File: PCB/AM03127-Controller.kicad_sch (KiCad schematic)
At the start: 13 parts, among them U1 XIAO-ESP32-C3-DIP, U2 MAX3232, U3 AMS1117 5.0

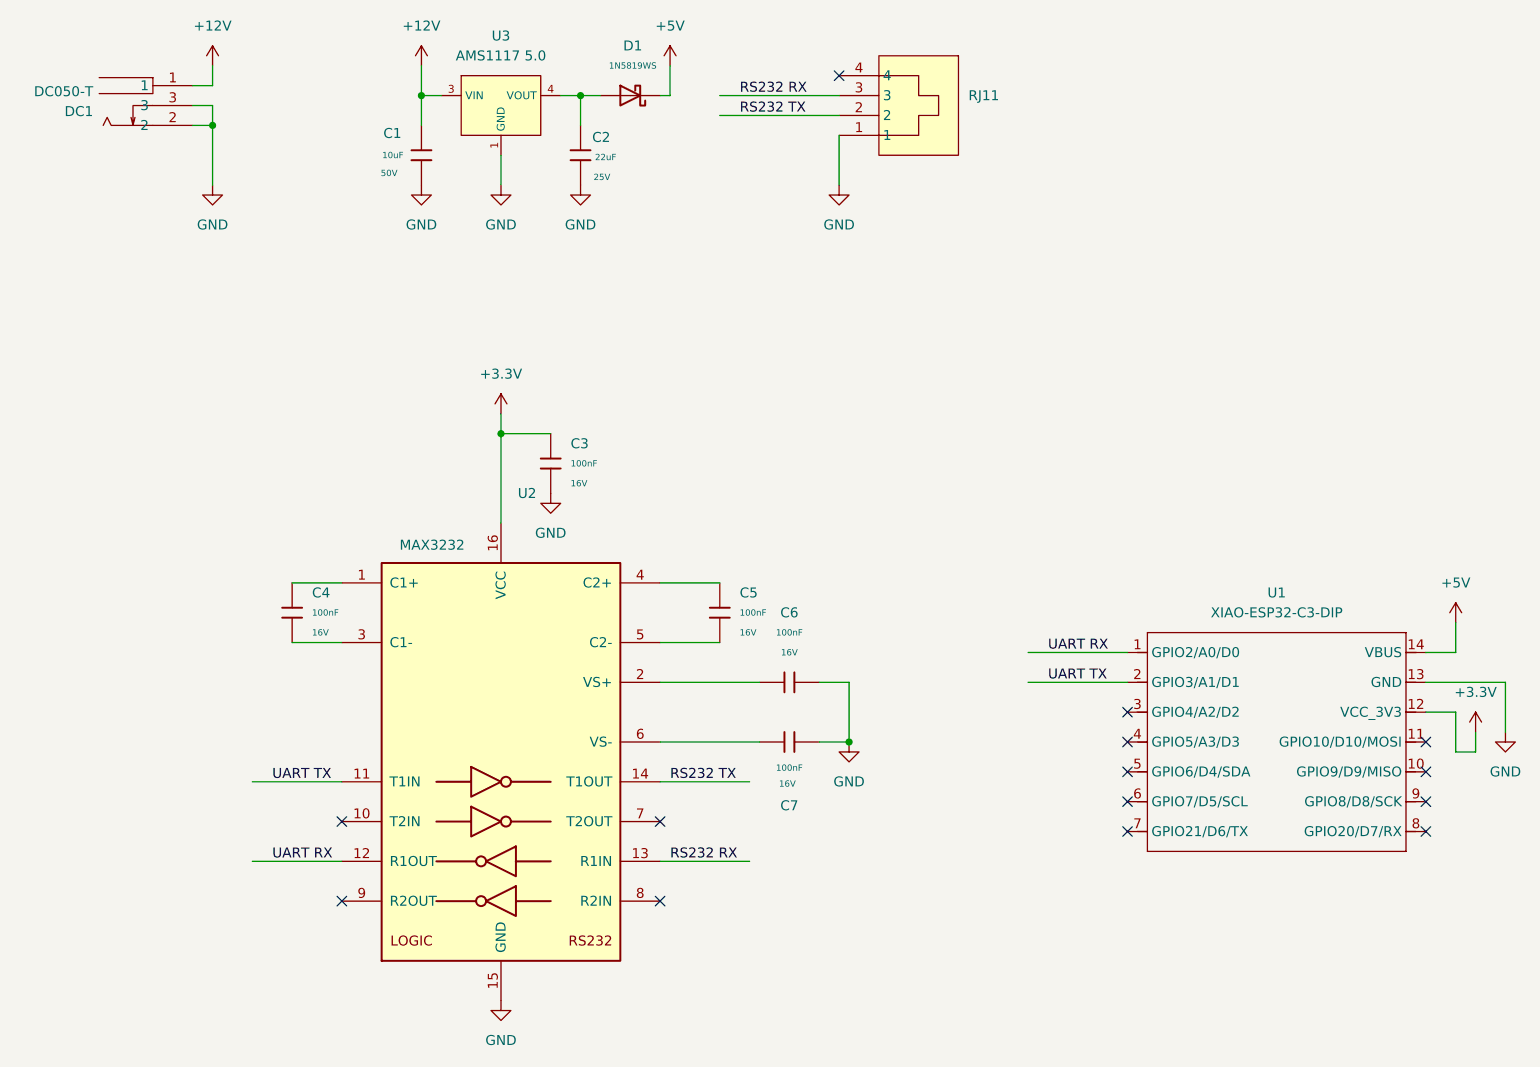
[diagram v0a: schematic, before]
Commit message: Refactor LDO to Buckconverter
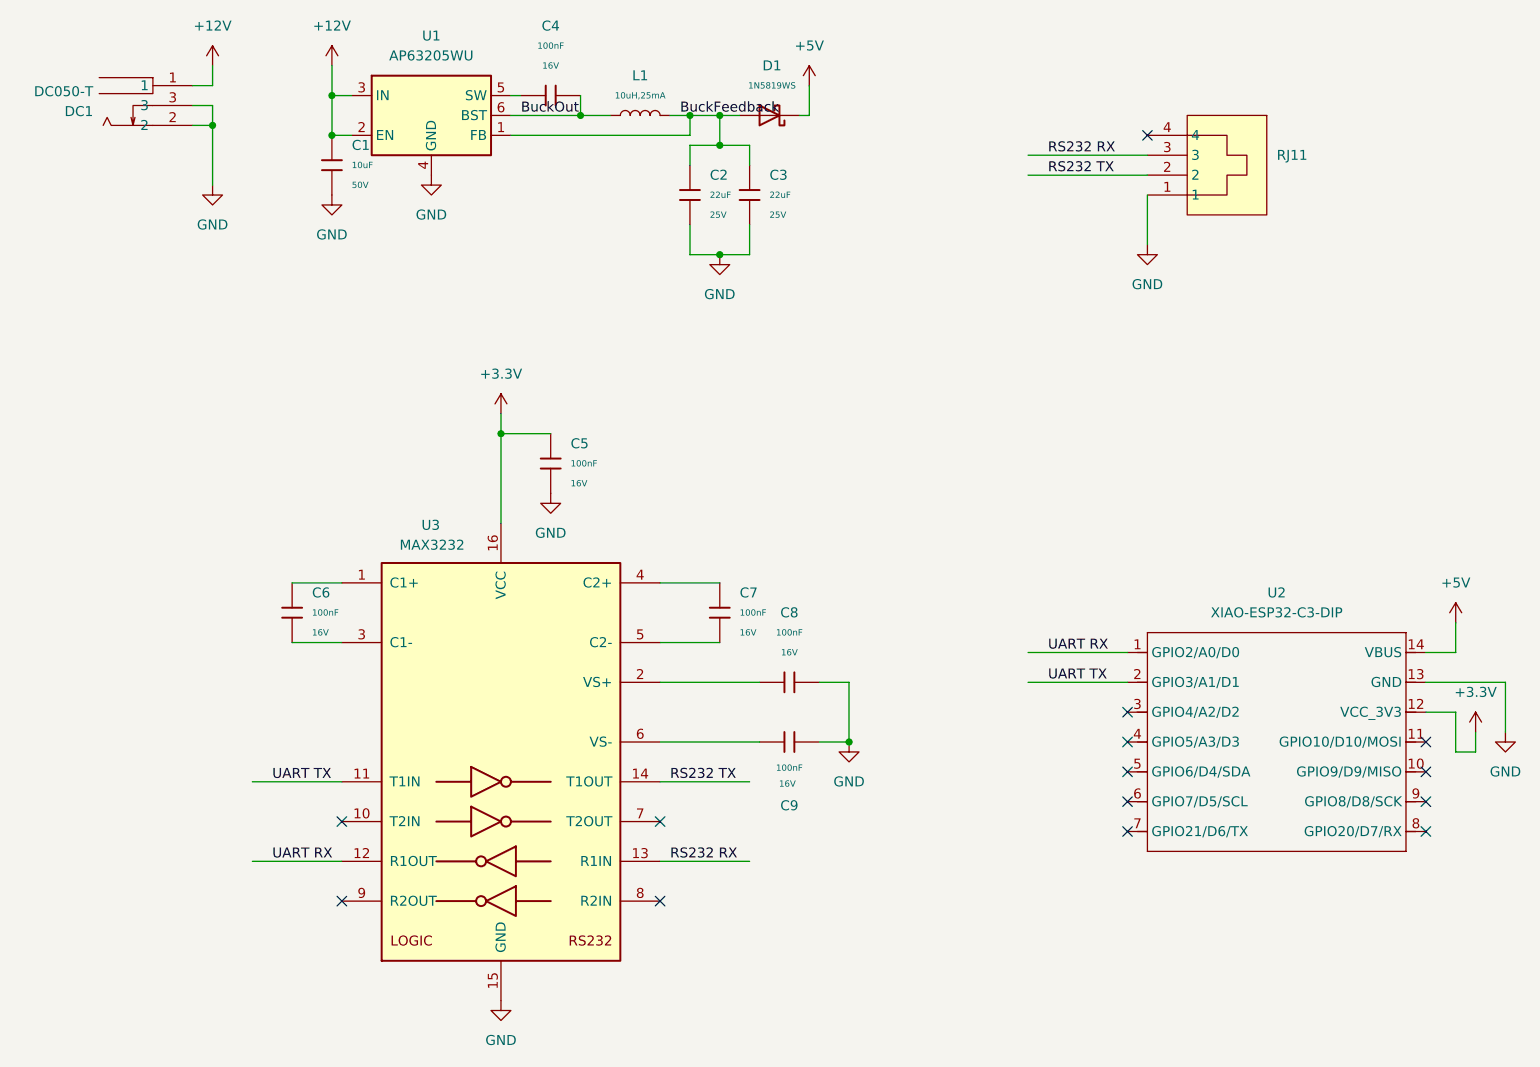
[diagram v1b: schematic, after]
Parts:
- removed C1: 10uF, PCM_JLCPCB:C_1206, symbol PCM_JLCPCB-Capacitors:1206,10uF
- removed C2: 22uF, PCM_JLCPCB:C_1206, symbol PCM_JLCPCB-Capacitors:1206,22uF,(2)
- removed U3: AMS1117 5.0, PCM_JLCPCB:SOT-223_L6.5-W3.5-P2.30-LS7.0-BR, symbol PCM_JLCPCB-Power:LDO, 5V, 1A
- added C1: 10uF, PCM_JLCPCB:C_0805, symbol PCM_JLCPCB-Capacitors:0805,10uF,(2)
- added C2, C3: 22uF, PCM_JLCPCB:C_0805, symbol PCM_JLCPCB-Capacitors:0805,22uF
- added C4: 100nF, PCM_JLCPCB:C_0402, symbol PCM_JLCPCB-Capacitors:0402,100nF
- added L1: 10uH,25mA, PCM_JLCPCB:L_1206, symbol PCM_JLCPCB-Inductors:10uH,25mA
- added U1: AP63205WU, Package_TO_SOT_SMD:TSOT-23-6, symbol Regulator_Switching:AP63205WU
- renumbered C3 to C5, C4 to C6, C5 to C7, C6 to C8, C7 to C9, U1 to U2, U2 to U3
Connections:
- net +12V: now also C1.1, U1.2 (EN), U1.3 (IN)
- net GND: now also C1.2, C2.2, C3.2, U1.4 (GND)
- net BuckFeedback: now reaches D1.2
- net BuckFeedback: now also C2.1, C3.1, L1.2, U1.1 (FB)
- new net: C4.1, U1.5 (SW)
- new net BuckOut: C4.2, L1.1, U1.6 (BST)
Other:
- moved on the sheet: D1, RJ11
